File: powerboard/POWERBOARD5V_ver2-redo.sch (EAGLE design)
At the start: 53 parts, among them IC1 TPS5420, IC2 TPS5420

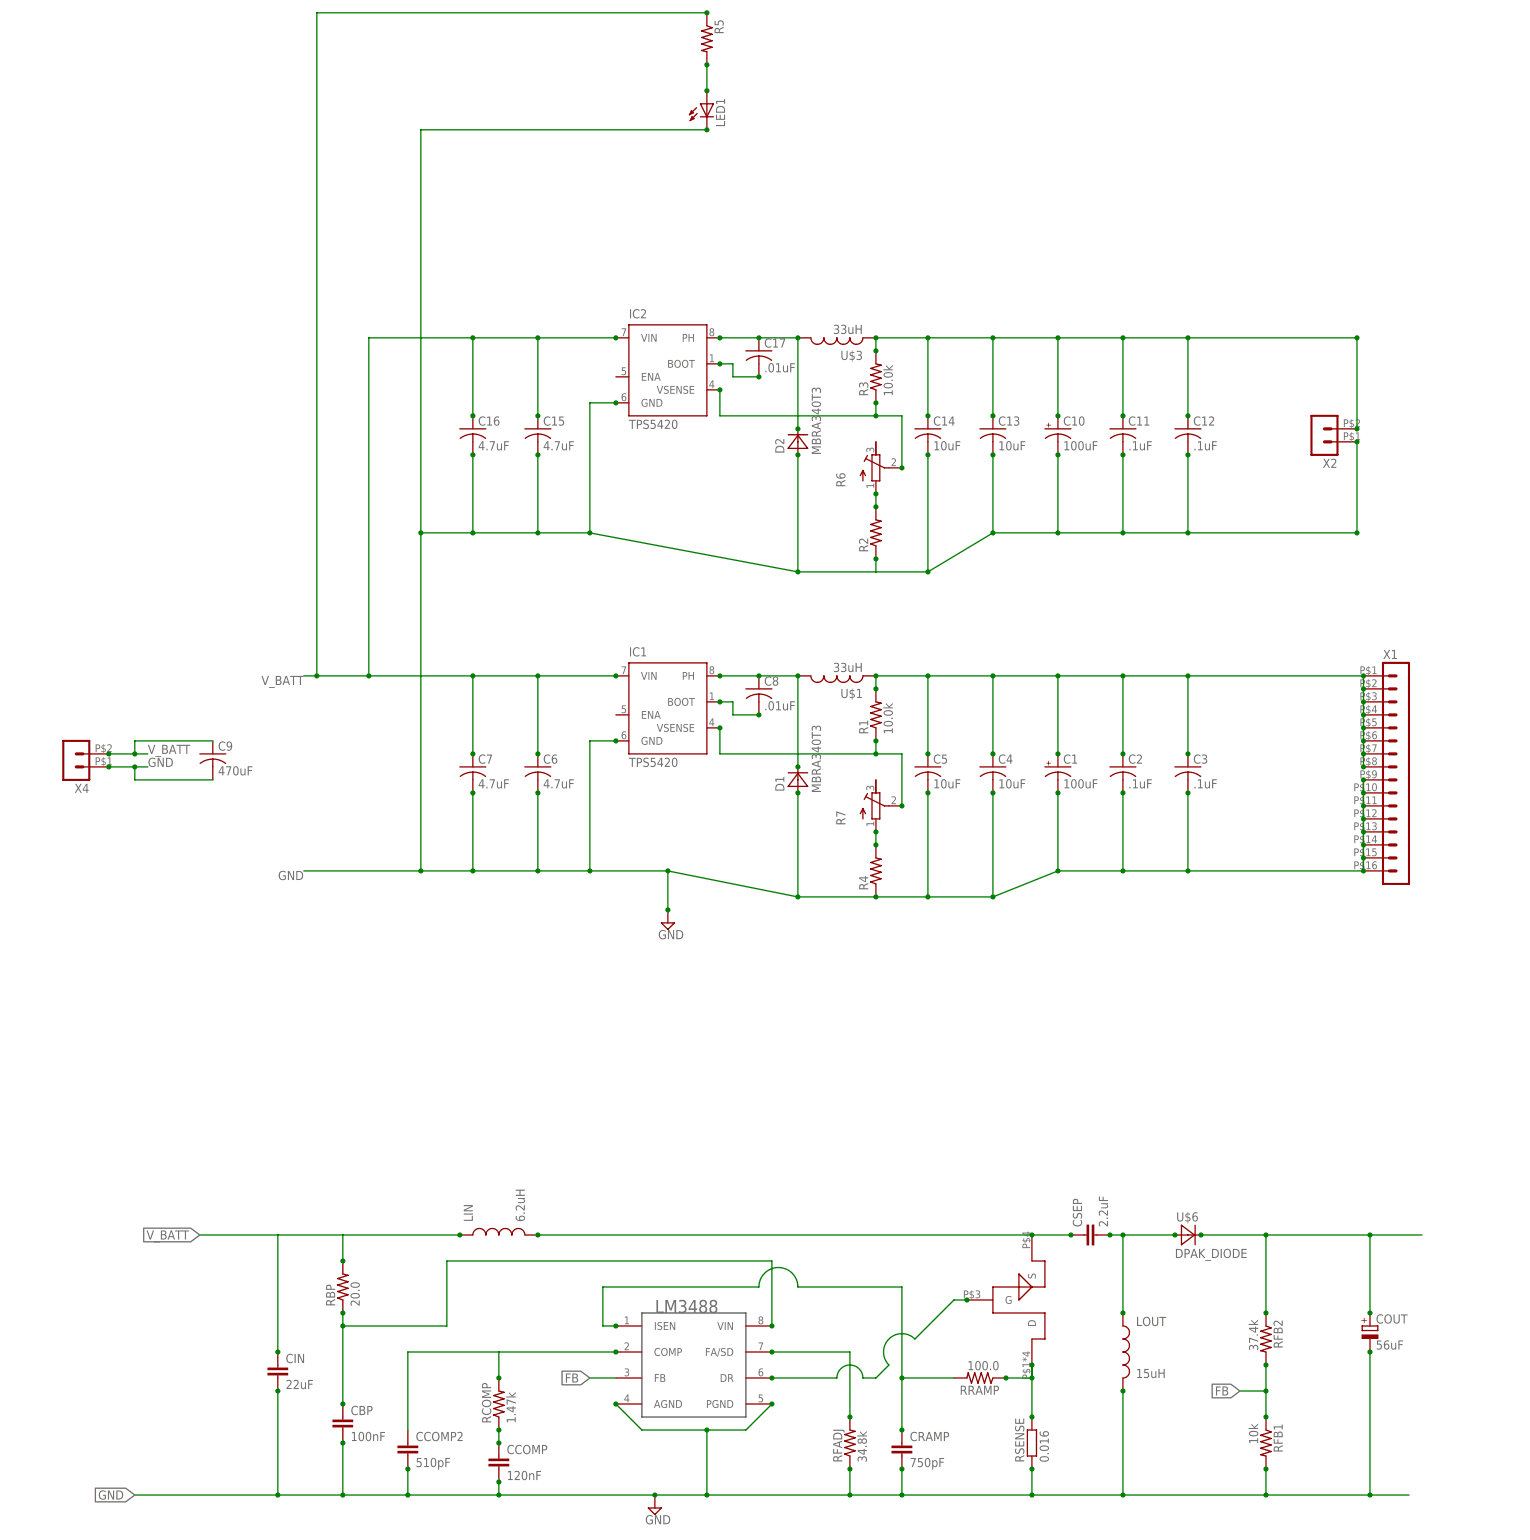
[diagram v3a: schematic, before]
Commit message: Finished layout of power board with 6V.
-Does not include new connectors for 3.3 and 5v rail yet
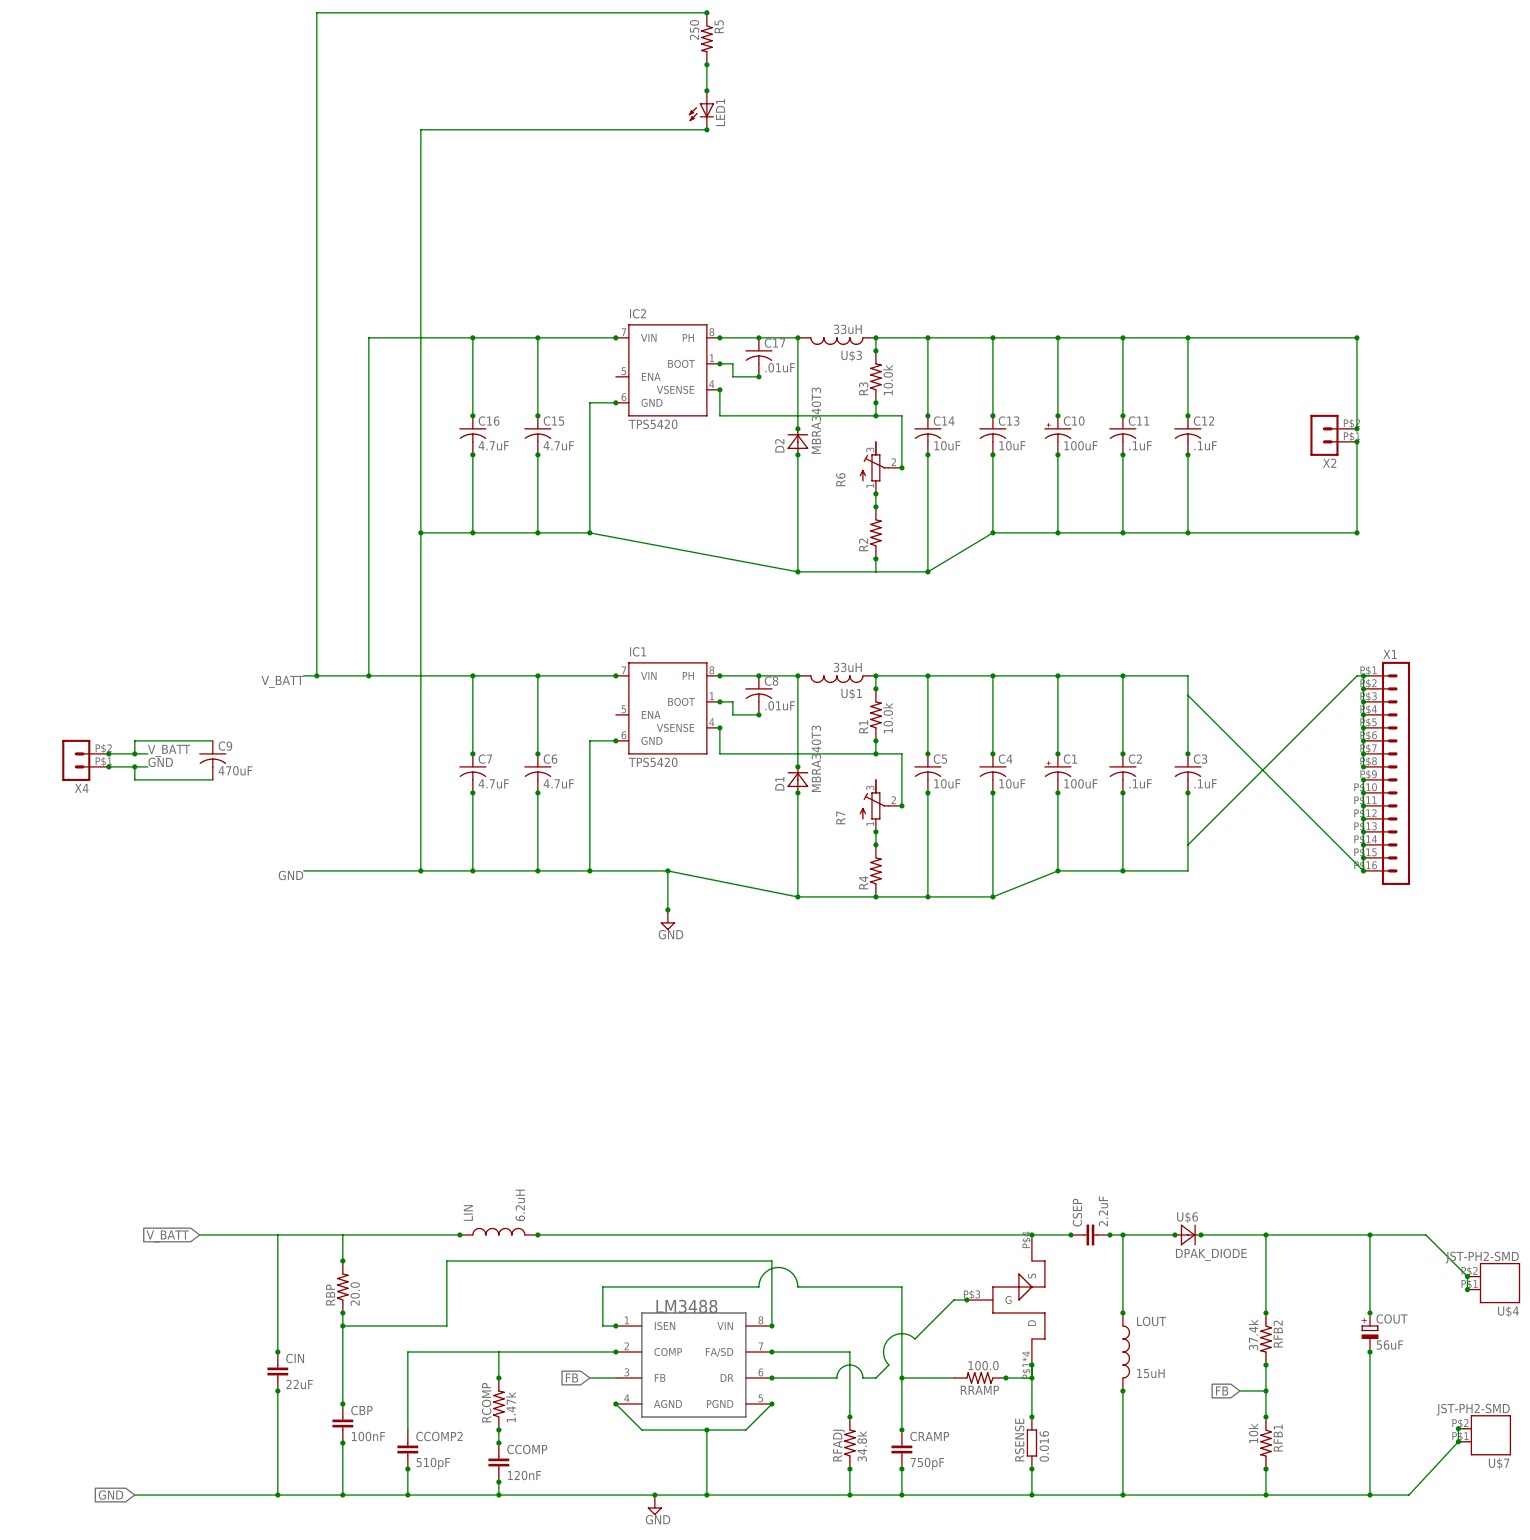
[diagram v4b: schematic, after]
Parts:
- added U$4, U$7: JST-PH2-SMD, jst-ph:JST-PH2-SMD
- R5: value (none) -> 250
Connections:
- net N$22 renamed SIG1
- net N$24 renamed LINSIG
- net N$25 renamed LSIG
- removed net N$26: COUT.+, RFB2.1, U$6.C
- new net 6V: COUT.+, RFB2.1, U$4.1, U$4.2, U$6.C
- net 5V: now also X1.10, X1.11, X1.12, X1.13, X1.14, X1.15, X1.16, X1.9; no longer X1.1, X1.2, X1.3, X1.4, X1.5, X1.6, X1.7, X1.8
- net GND: now also U$7.1, U$7.2, X1.1, X1.2, X1.3, X1.4, X1.5, X1.6, X1.7, X1.8; no longer X1.10, X1.11, X1.12, X1.13, X1.14, X1.15, X1.16, X1.9

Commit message: Added 2nd 56uF cap to powerboard, finished, needs DRC
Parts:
- added COUT1: 56uF, rcl:CPOL-EUSANYO_SMD_A5
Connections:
- net 6V: now also COUT1.+
- net GND: now also COUT1.-
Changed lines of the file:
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@@
 <setting verticaltext="up"/>
 </settings>
-<grid distance="0.01" unitdist="inch" unit="inch" style="lines" multiple="1" display="no" altdistance="0.01" altunitdist="inch" altunit="inch"/>
+<grid distance="0.1" unitdist="inch" unit="inch" style="lines" multiple="1" display="no" altdistance="0.01" altunitdist="inch" altunit="inch"/>
 <layers>
 <layer number="1" name="Top" color="4" fill="1" visible="no" active="no"/>
@@
 <part name="U$4" library="jst-ph" deviceset="JST-PH2-SMD" device=""/>
 <part name="U$7" library="jst-ph" deviceset="JST-PH2-SMD" device=""/>
+<part name="COUT1" library="rcl" deviceset="CPOL-EU" device="SANYO_SMD_A5" value="56uF"/>
 </parts>
 <sheets>
@@
 <instance part="U$4" gate="G$1" x="194.31" y="-99.568" rot="R180"/>
 <instance part="U$7" gate="G$1" x="192.532" y="-129.286" rot="R180"/>
+<instance part="COUT1" gate="G$1" x="162.56" y="-106.68" rot="MR0"/>
 </instances>
 <busses>
@@
 <junction x="184.912" y="-129.286"/>
 <junction x="184.912" y="-126.746"/>
+<pinref part="COUT1" gate="G$1" pin="-"/>
+<wire x1="162.56" y1="-111.76" x2="167.64" y2="-111.76" width="0.1524" layer="91"/>
+<junction x="162.56" y="-111.76"/>
 </segment>
 <segment>
@@
 <junction x="186.69" y="-97.028"/>
 <junction x="186.69" y="-99.568"/>
-</segment>
-</net>
+<pinref part="COUT1" gate="G$1" pin="+"/>
+<wire x1="167.64" y1="-104.14" x2="162.56" y2="-104.14" width="0.1524" layer="91"/>
+<junction x="162.56" y="-104.14"/>
+</segment>
+</net>

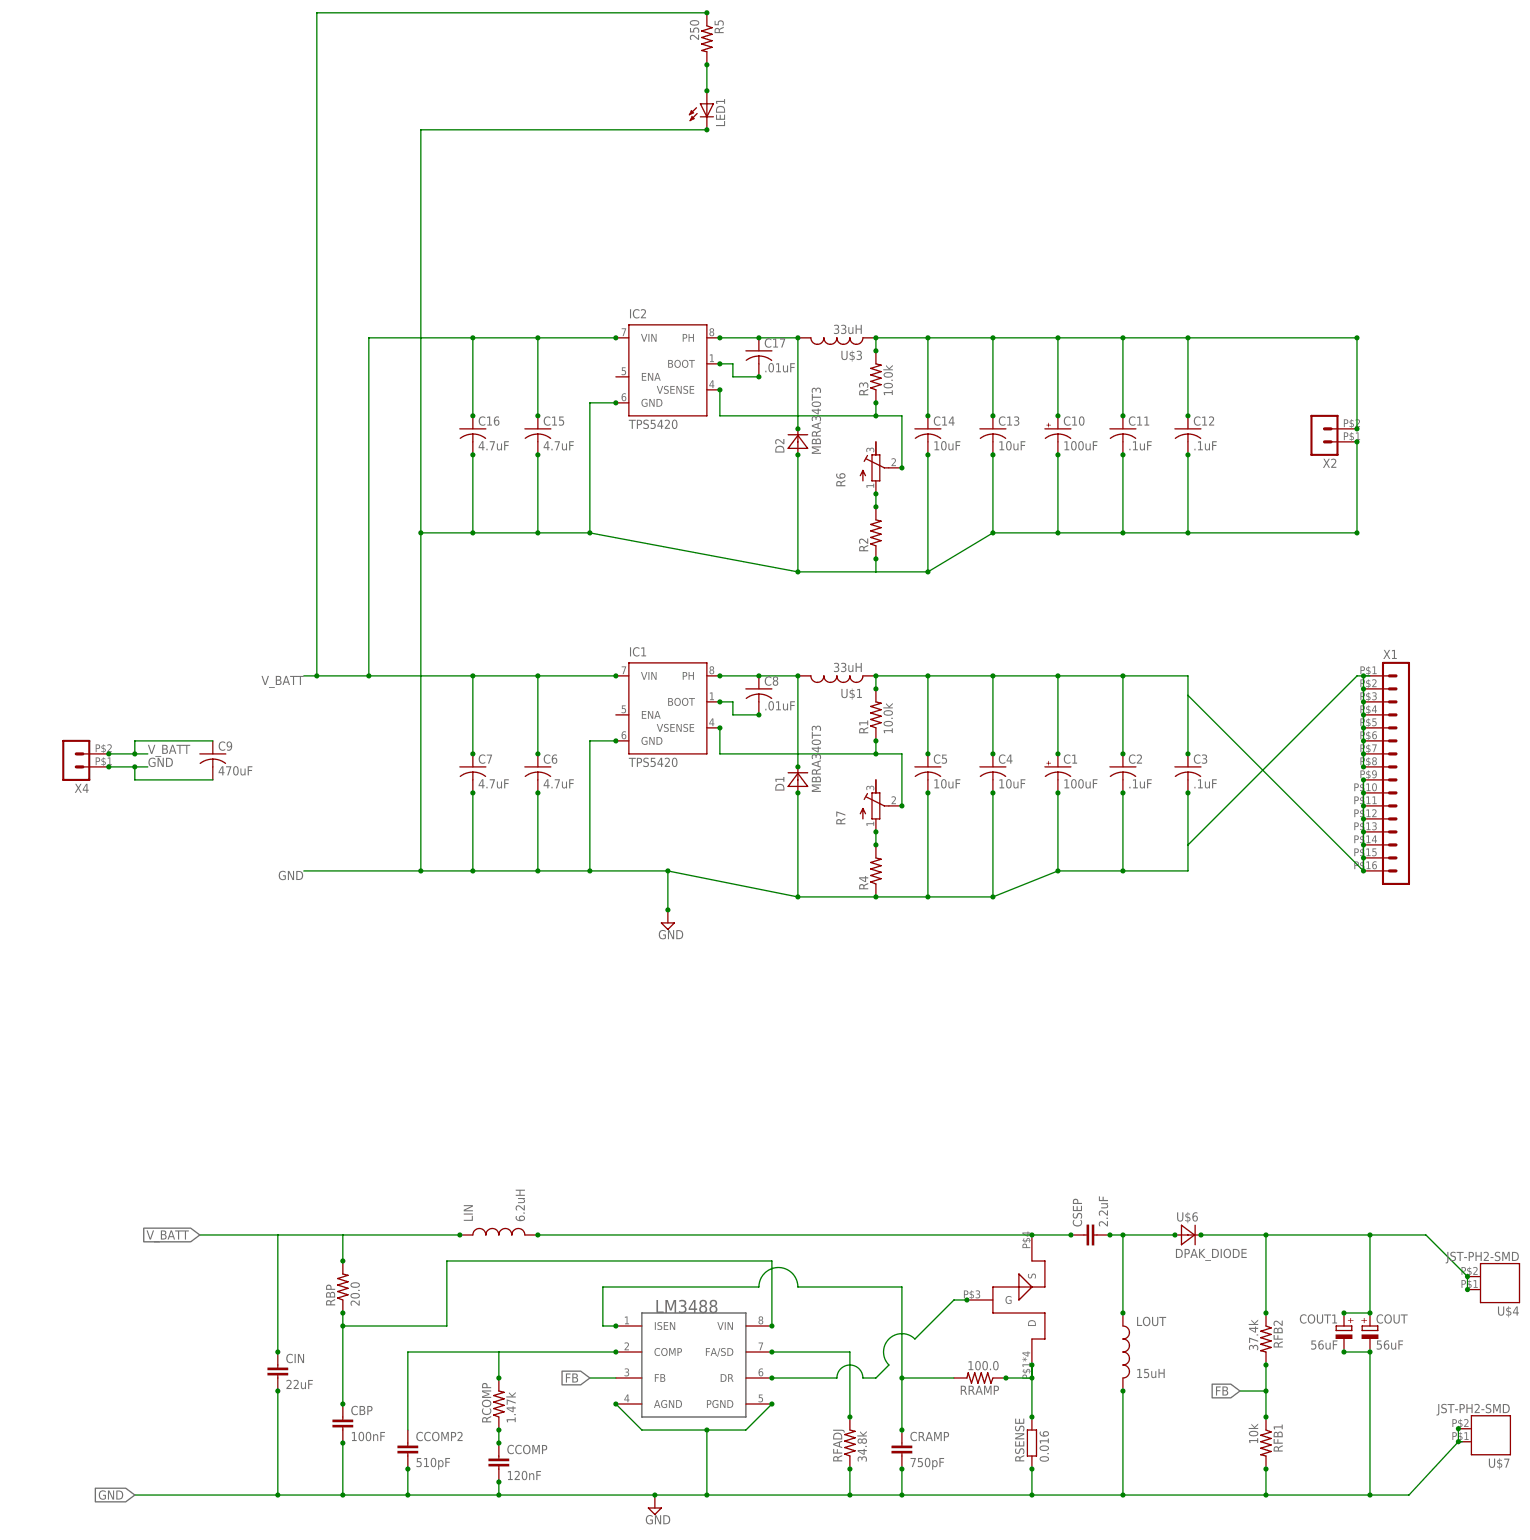
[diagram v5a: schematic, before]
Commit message: fixed fet, and fixed connector type
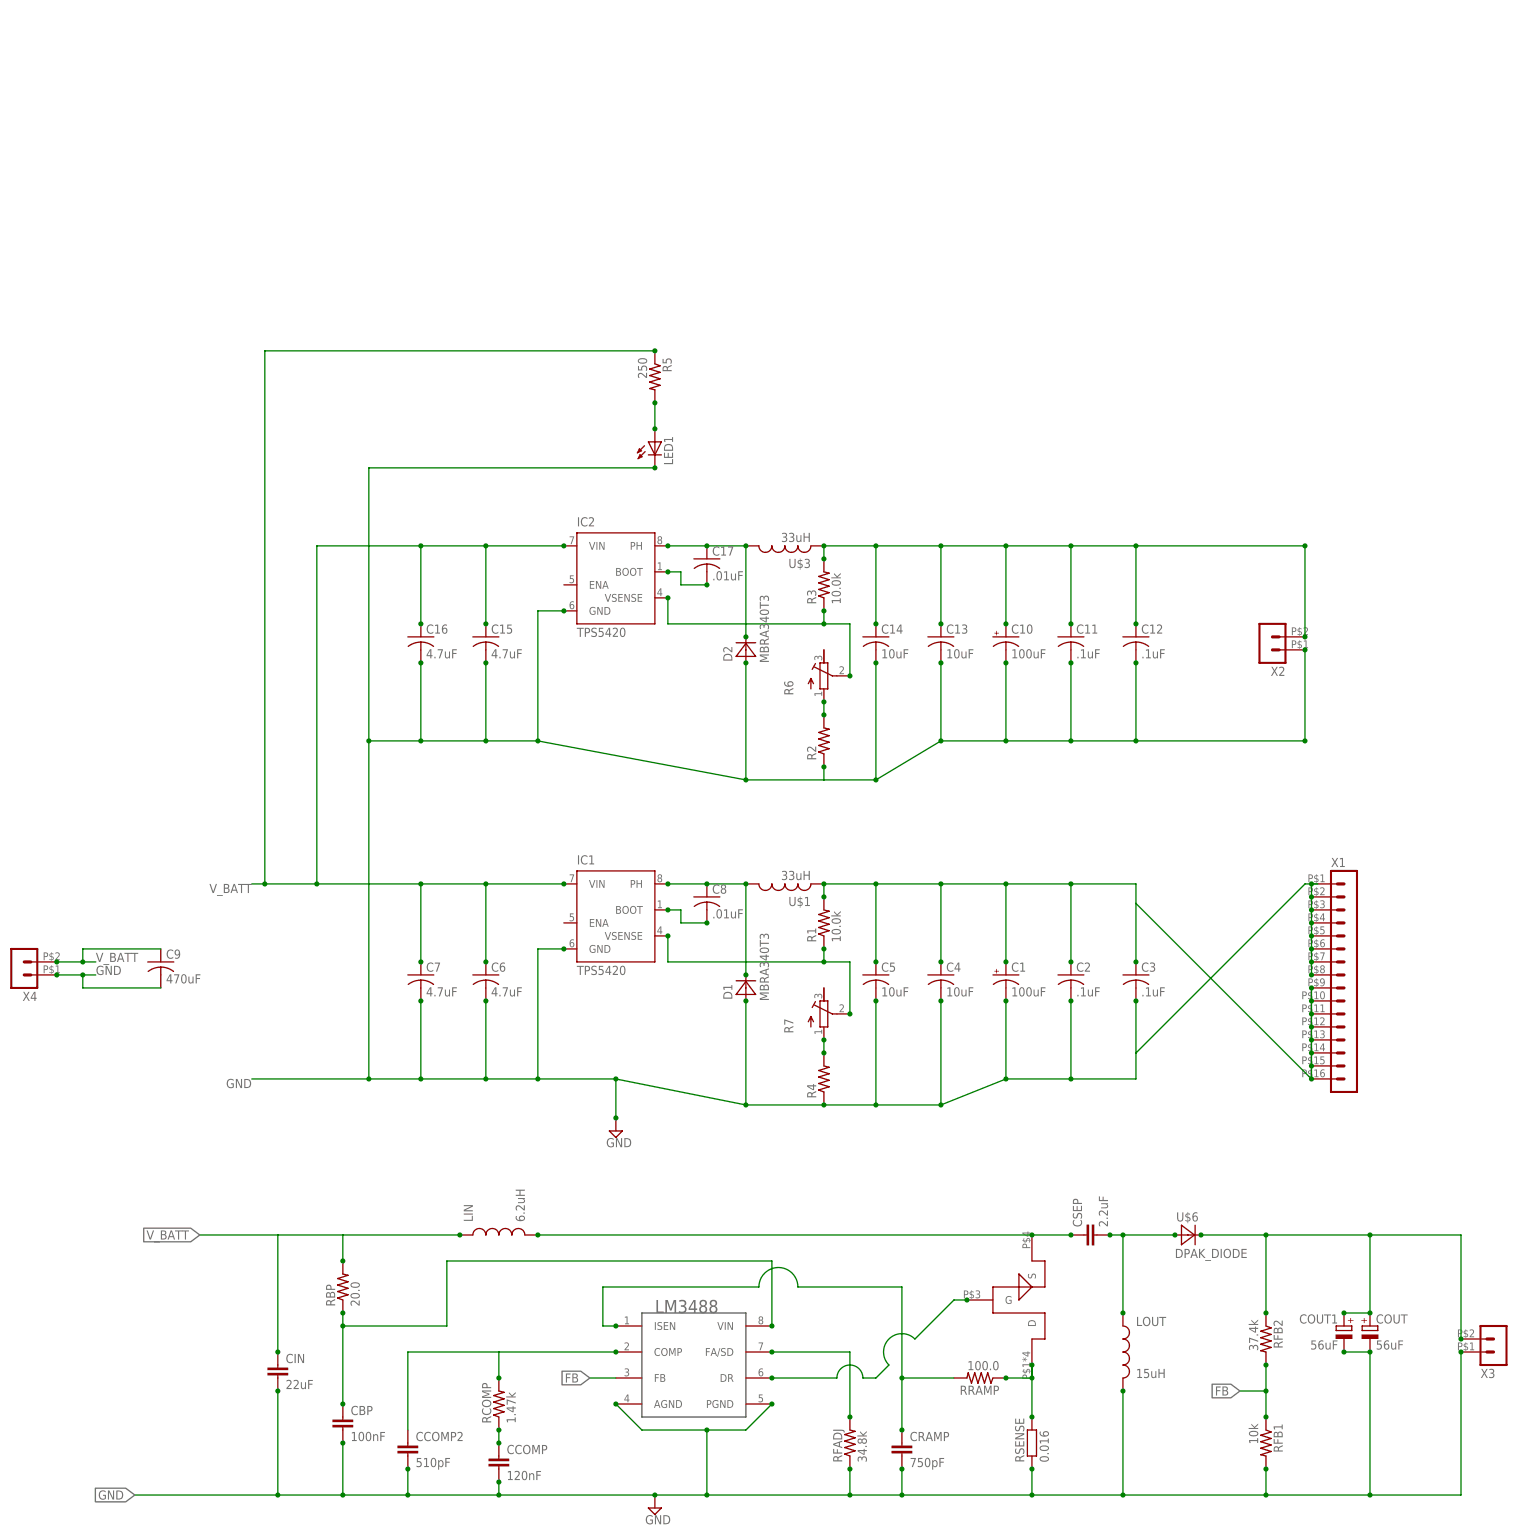
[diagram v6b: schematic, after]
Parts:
- removed U$4, U$7: JST-PH2-SMD, jst-ph:JST-PH2-SMD
- added X3: (no value), con-molex-micro-fit-3_0:HEADER_POS2_43045-0206
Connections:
- net 6V: now also X3.2; no longer U$4.1, U$4.2
- net GND: now also X3.1; no longer U$7.1, U$7.2
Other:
- moved on the sheet: C1, C10, C11, C12, C13, C14, C15, C16, C17, C2, C3, C4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
